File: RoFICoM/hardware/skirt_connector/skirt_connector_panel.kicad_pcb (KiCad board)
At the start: 2 copper layers, 100 x 100 mm, 153 parts, among them J1 Cable, J10 SENSE_1, J11 SENSE_2, J12 48V_B, J13 48V_2, J14 GND_B, J15 GND_2, J16 RX_B, J17 TX_2, J2 48V_A, J3 48V_1, J4 GND_A, J5 GND_1, J6 RX_A, J7 TX_1, J8 SENSE_A, J9 SENSE_B

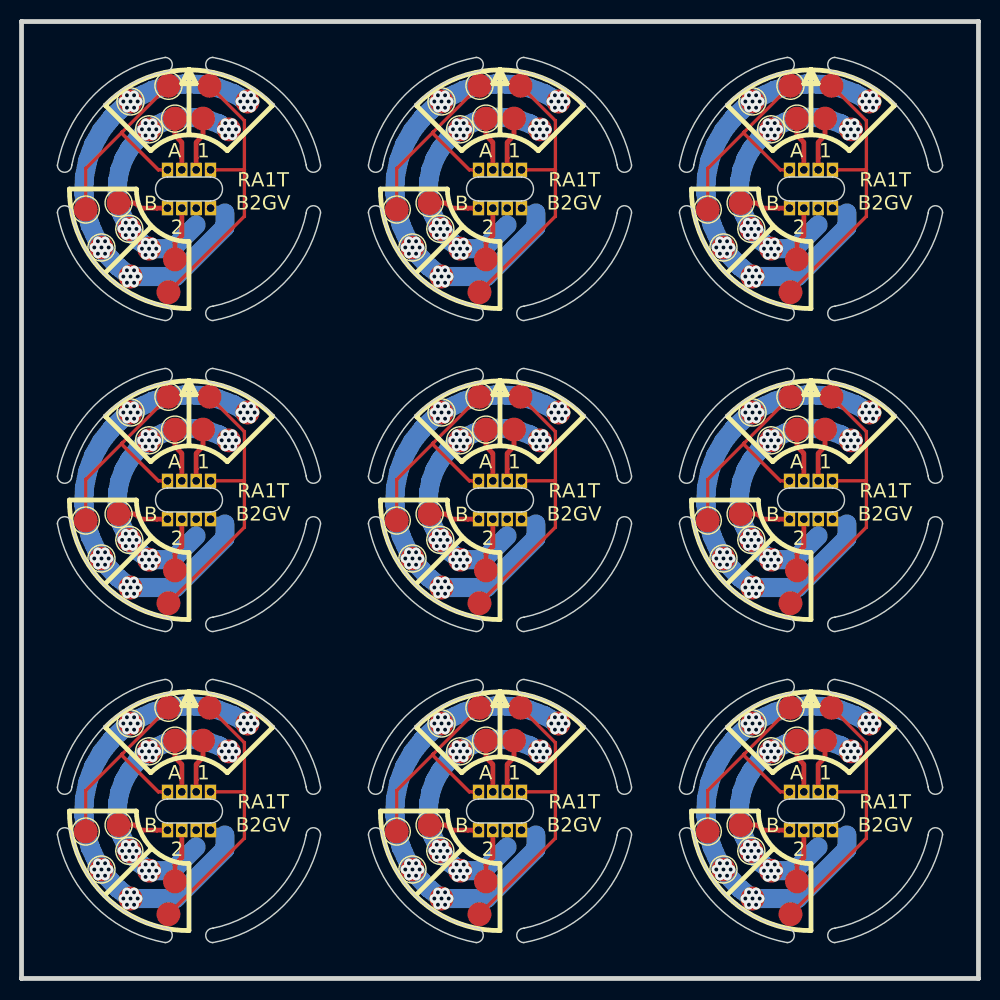
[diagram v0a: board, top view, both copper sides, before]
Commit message: RoFICoM: Update skirt connector panel
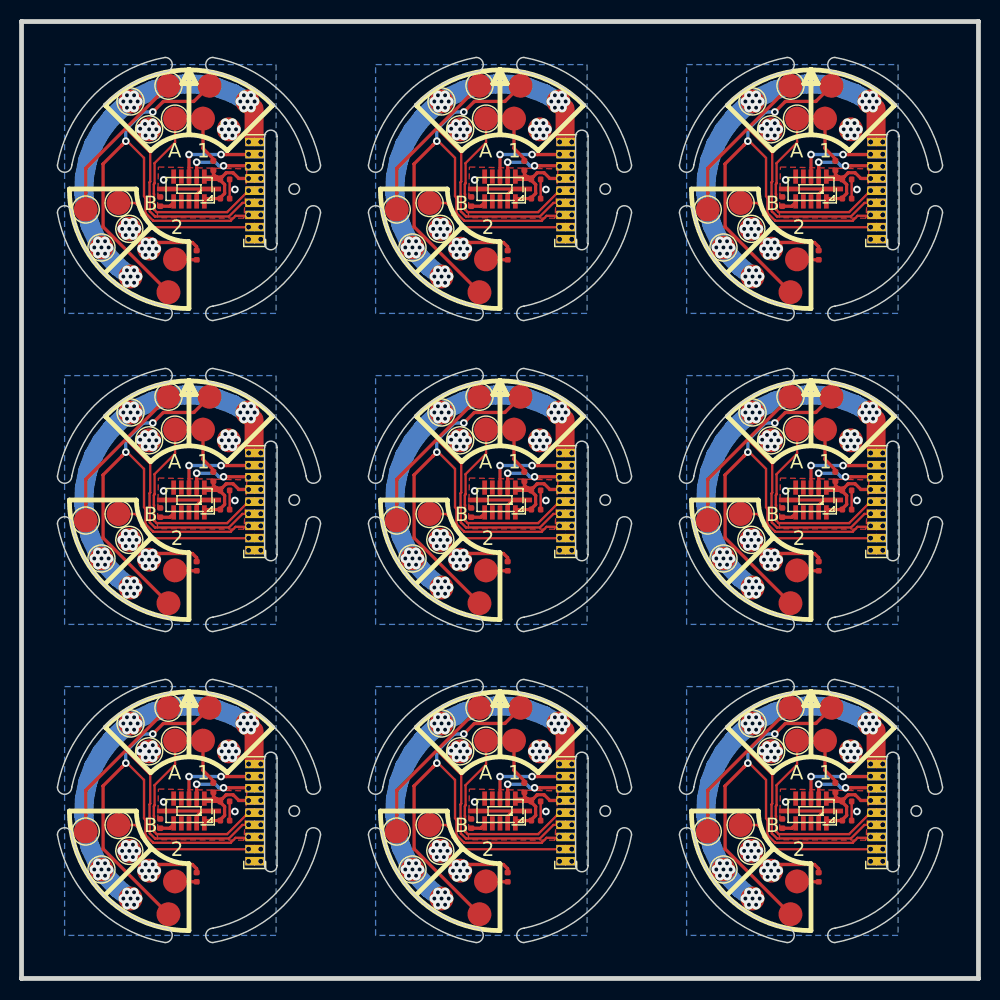
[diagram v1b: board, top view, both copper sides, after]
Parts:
- removed the J1 at (217.5, 167.5)
- removed the J1 at (185.0, 167.5)
- removed the J1 at (152.5, 167.5)
- removed the J1 at (185.0, 135.0)
- removed the J1 at (152.5, 135.0)
- removed the J1 at (217.5, 135.0)
- removed the J1 at (217.5, 102.5)
- removed the J1 at (185.0, 102.5)
- removed the J1 at (152.5, 102.5)
- added C1: 470n, Capacitor_SMD:C_0402_1005Metric, F.Cu at (221.3, 168.5)
- added C1: 470n, Capacitor_SMD:C_0402_1005Metric, F.Cu at (188.8, 168.5)
- added C1: 470n, Capacitor_SMD:C_0402_1005Metric, F.Cu at (156.3, 168.5)
- added C1: 470n, Capacitor_SMD:C_0402_1005Metric, F.Cu at (156.3, 136.0)
- added C1: 470n, Capacitor_SMD:C_0402_1005Metric, F.Cu at (188.8, 136.0)
- added C1: 470n, Capacitor_SMD:C_0402_1005Metric, F.Cu at (221.3, 136.0)
- added C1: 470n, Capacitor_SMD:C_0402_1005Metric, F.Cu at (221.3, 103.5)
- added C1: 470n, Capacitor_SMD:C_0402_1005Metric, F.Cu at (188.8, 103.5)
- added C1: 470n, Capacitor_SMD:C_0402_1005Metric, F.Cu at (156.3, 103.5)
- added C2: 100n, Capacitor_SMD:C_0402_1005Metric, F.Cu at (221.3, 166.5)
- added C2: 100n, Capacitor_SMD:C_0402_1005Metric, F.Cu at (188.8, 166.5)
- added C2: 100n, Capacitor_SMD:C_0402_1005Metric, F.Cu at (156.3, 166.5)
- added C2: 100n, Capacitor_SMD:C_0402_1005Metric, F.Cu at (156.3, 134.0)
- added C2: 100n, Capacitor_SMD:C_0402_1005Metric, F.Cu at (188.8, 134.0)
- added C2: 100n, Capacitor_SMD:C_0402_1005Metric, F.Cu at (221.3, 134.0)
- added C2: 100n, Capacitor_SMD:C_0402_1005Metric, F.Cu at (221.3, 101.5)
- added C2: 100n, Capacitor_SMD:C_0402_1005Metric, F.Cu at (188.8, 101.5)
- added C2: 100n, Capacitor_SMD:C_0402_1005Metric, F.Cu at (156.3, 101.5)
- added J1: Cable, rofi:flat_cable_9, F.Cu at (225.0, 172.8)
- added J1: Cable, rofi:flat_cable_9, F.Cu at (192.5, 172.8)
- added J1: Cable, rofi:flat_cable_9, F.Cu at (160.0, 172.8)
- added J1: Cable, rofi:flat_cable_9, F.Cu at (160.0, 140.2)
- added J1: Cable, rofi:flat_cable_9, F.Cu at (192.5, 140.2)
- added J1: Cable, rofi:flat_cable_9, F.Cu at (225.0, 140.2)
- added J1: Cable, rofi:flat_cable_9, F.Cu at (225.0, 107.8)
- added J1: Cable, rofi:flat_cable_9, F.Cu at (192.5, 107.8)
- added J1: Cable, rofi:flat_cable_9, F.Cu at (160.0, 107.8)
- added R1: 10k, Resistor_SMD:R_0402_1005Metric, F.Cu at (214.5, 168.8)
- added R1: 10k, Resistor_SMD:R_0402_1005Metric, F.Cu at (182.0, 168.8)
- added R1: 10k, Resistor_SMD:R_0402_1005Metric, F.Cu at (149.5, 168.8)
- added R1: 10k, Resistor_SMD:R_0402_1005Metric, F.Cu at (149.5, 136.3)
- added R1: 10k, Resistor_SMD:R_0402_1005Metric, F.Cu at (182.0, 136.3)
- added R1: 10k, Resistor_SMD:R_0402_1005Metric, F.Cu at (214.5, 136.3)
- added R1: 10k, Resistor_SMD:R_0402_1005Metric, F.Cu at (214.5, 103.8)
- added R1: 10k, Resistor_SMD:R_0402_1005Metric, F.Cu at (182.0, 103.8)
- added R1: 10k, Resistor_SMD:R_0402_1005Metric, F.Cu at (149.5, 103.8)
- added R2: 10k, Resistor_SMD:R_0402_1005Metric, F.Cu at (220.1, 165.1)
- added R2: 10k, Resistor_SMD:R_0402_1005Metric, F.Cu at (187.6, 165.1)
- added R2: 10k, Resistor_SMD:R_0402_1005Metric, F.Cu at (155.1, 165.1)
- added R2: 10k, Resistor_SMD:R_0402_1005Metric, F.Cu at (155.1, 132.6)
- added R2: 10k, Resistor_SMD:R_0402_1005Metric, F.Cu at (187.6, 132.6)
- added R2: 10k, Resistor_SMD:R_0402_1005Metric, F.Cu at (220.1, 132.6)
- added R2: 10k, Resistor_SMD:R_0402_1005Metric, F.Cu at (220.1, 100.0)
- added R2: 10k, Resistor_SMD:R_0402_1005Metric, F.Cu at (187.6, 100.0)
- added R2: 10k, Resistor_SMD:R_0402_1005Metric, F.Cu at (155.1, 100.0)
- added R3: 10k, Resistor_SMD:R_0402_1005Metric, F.Cu at (218.3, 174.4)
- added R3: 10k, Resistor_SMD:R_0402_1005Metric, F.Cu at (185.8, 174.4)
- added R3: 10k, Resistor_SMD:R_0402_1005Metric, F.Cu at (153.3, 174.4)
- added R3: 10k, Resistor_SMD:R_0402_1005Metric, F.Cu at (153.3, 141.9)
- added R3: 10k, Resistor_SMD:R_0402_1005Metric, F.Cu at (185.8, 141.9)
- added R3: 10k, Resistor_SMD:R_0402_1005Metric, F.Cu at (218.3, 141.9)
- added R3: 10k, Resistor_SMD:R_0402_1005Metric, F.Cu at (218.3, 109.4)
- added R3: 10k, Resistor_SMD:R_0402_1005Metric, F.Cu at (185.8, 109.4)
- added R3: 10k, Resistor_SMD:R_0402_1005Metric, F.Cu at (153.3, 109.4)
- added U1: VL53L1X, rofi:VL53L1X_handsoldering, F.Cu at (217.5, 167.5)
- added U1: VL53L1X, rofi:VL53L1X_handsoldering, F.Cu at (185.0, 167.5)
- added U1: VL53L1X, rofi:VL53L1X_handsoldering, F.Cu at (152.5, 167.5)
- added U1: VL53L1X, rofi:VL53L1X_handsoldering, F.Cu at (152.5, 135.0)
- added U1: VL53L1X, rofi:VL53L1X_handsoldering, F.Cu at (185.0, 135.0)
- added U1: VL53L1X, rofi:VL53L1X_handsoldering, F.Cu at (217.5, 135.0)
- added U1: VL53L1X, rofi:VL53L1X_handsoldering, F.Cu at (217.5, 102.5)
- added U1: VL53L1X, rofi:VL53L1X_handsoldering, F.Cu at (185.0, 102.5)
- added U1: VL53L1X, rofi:VL53L1X_handsoldering, F.Cu at (152.5, 102.5)
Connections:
- net 48V renamed +48V
- net S_1_PAD renamed Net-(J10-Pad1)
- net S_2_PAD renamed Net-(J11-Pad1)
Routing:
- net TX: track 269.3 -> 472.8 mm, vias 0 -> 18
- net GND: track 281.1 -> 120.0 mm, vias 252 -> 270
- net S_A_PIN: track 50.9 -> 205.2 mm
- net RX: track 206.8 -> 348.8 mm
- net +3V3: track 0.00 -> 117.0 mm
- net S_B_PIN: track 48.0 -> 157.7 mm
- net SDA: track 0.00 -> 105.5 mm, vias 0 -> 18
- net SCL: track 0.00 -> 92.6 mm, vias 0 -> 18
- net +48V: track 448.0 -> 361.5 mm
- net Net-(J11-Pad1): track 50.9 -> 21.6 mm
- net Net-(R1-Pad1): track 0.00 -> 14.1 mm
- net Net-(J10-Pad1): track 50.9 -> 41.9 mm
- added copper zone on B.Cu, net GND
- added copper zone on F.Cu, net GND
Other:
- outline, holes or cut-outs redrawn
- board text added: "RoFICoM Skirt v0.2 03/2019"
- board text removed: "RA1T B2GV"
- board text removed: "RoFI - DockSkirt v0.1 12/2018"
